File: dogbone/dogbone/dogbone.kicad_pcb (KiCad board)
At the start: 2 copper layers, 23 x 27.4 mm, 11 parts, among them J1 jstsh4x1, U1 TLV2771CDBVT

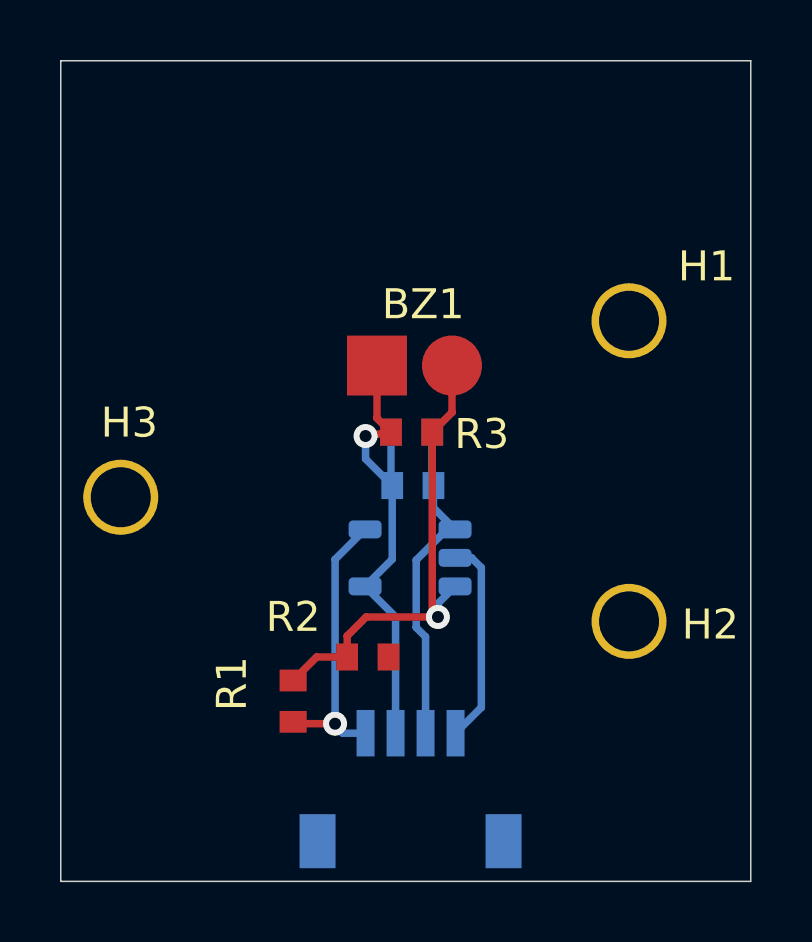
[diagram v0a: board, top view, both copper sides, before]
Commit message: added grbl files for dogbone, and update csv
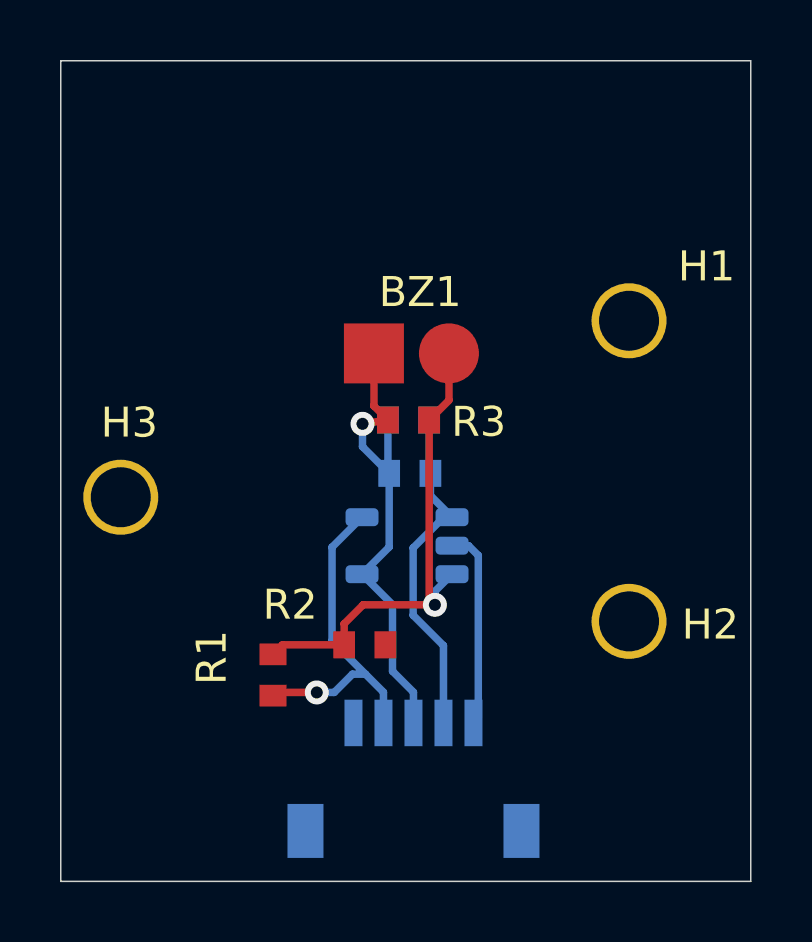
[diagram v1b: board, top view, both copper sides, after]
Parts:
- J1: value jstsh4x1 -> jstsh5x1; footprint exocam_charge_amp:jstsh4x1 -> exocam_charge_amp:jstsh5x1
- moved R1 1.10 mm to (49.1, 96.0)
- moved J1 0.69 mm to (55.5, 95.6)
- moved C1 0.42 mm to (56.8, 90.6)
- moved R3 0.42 mm to (55.6, 90.6)
- moved R2 0.42 mm to (55.3, 93.0)
- moved R4 0.42 mm to (56.8, 92.4)
- moved BZ1 0.42 mm to (56.6, 83.3)
- moved U1 0.42 mm to (56.3, 88.7)
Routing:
- net +3V3: track 9.55 -> 11.4 mm

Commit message: fixed dogbones
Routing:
- net GND: track 6.66 -> 9.92 mm, vias 0 -> 1
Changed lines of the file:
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@@
     (thickness 1.6)
     (drawings 4)
-    (tracks 53)
+    (tracks 57)
     (zones 0)
     (modules 11)
@@
       (effects (font (size 1 1) (thickness 0.15)) (justify mirror))
     )
+    (fp_line (start 3.185 -3) (end 3.185 -6.84) (layer Dwgs.User) (width 0.12))
+    (fp_line (start 3.185 -3) (end -4.805 -3) (layer Dwgs.User) (width 0.12))
+    (fp_line (start -4.805 -6.84) (end -4.805 -3) (layer Dwgs.User) (width 0.12))
     (fp_line (start -4.805 -6.84) (end 3.185 -6.84) (layer Dwgs.User) (width 0.12))
-    (fp_line (start -4.805 -6.84) (end -4.805 -3) (layer Dwgs.User) (width 0.12))
-    (fp_line (start 3.185 -3) (end -4.805 -3) (layer Dwgs.User) (width 0.12))
-    (fp_line (start 3.185 -3) (end 3.185 -6.84) (layer Dwgs.User) (width 0.12))
     (pad 5 smd rect (at 1.19 -2.54 180) (size 0.6 1.55) (layers B.Cu B.Paste B.Mask)
       (net 4 "Net-(J1-Pad5)"))
@@
   (segment (start 58.49491 92.56261) (end 58.1699 92.2376) (width 0.25) (layer B.Cu) (net 6))
   (segment (start 58.49491 97.98509) (end 58.3344 98.1456) (width 0.25) (layer B.Cu) (net 6))
-  (segment (start 58.49491 92.56261) (end 58.49491 97.98509) (width 0.25) (layer B.Cu) (net 6))
+  (segment (start 58.49491 92.56261) (end 58.49491 95.14969) (width 0.25) (layer B.Cu) (net 6))
+  (segment (start 58.49491 95.14969) (end 58.49491 97.98509) (width 0.25) (layer B.Cu) (net 6))
+  (via (at 58.49491 95.14969) (size 0.8) (drill 0.4) (layers F.Cu B.Cu) (net 6))
+  (segment (start 58.1025 95.5421) (end 58.49491 95.14969) (width 0.25) (layer F.Cu) (net 6))
+  (segment (start 55.3974 95.5421) (end 58.1025 95.5421) (width 0.25) (layer F.Cu) (net 6))
 )
